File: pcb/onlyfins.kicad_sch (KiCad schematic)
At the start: 47 parts, among them J2 12V_in, Q1 BSS138, U1 L7805

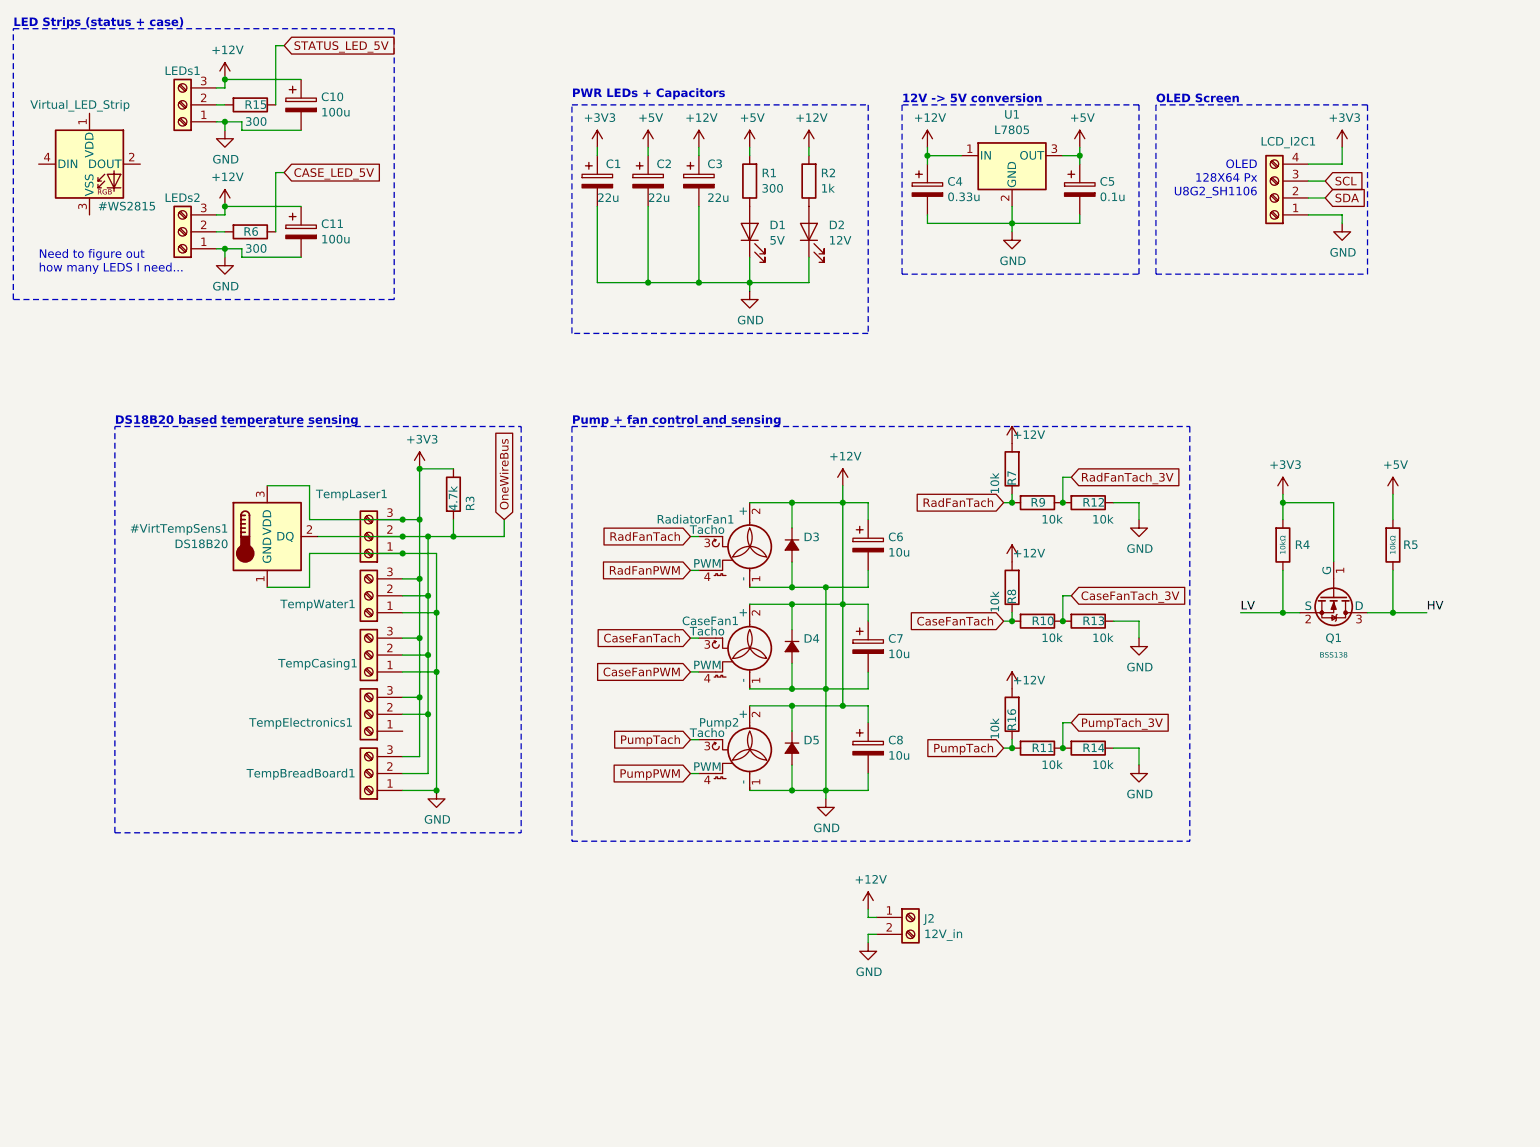
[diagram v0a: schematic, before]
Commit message: Adding subsheets for fan control
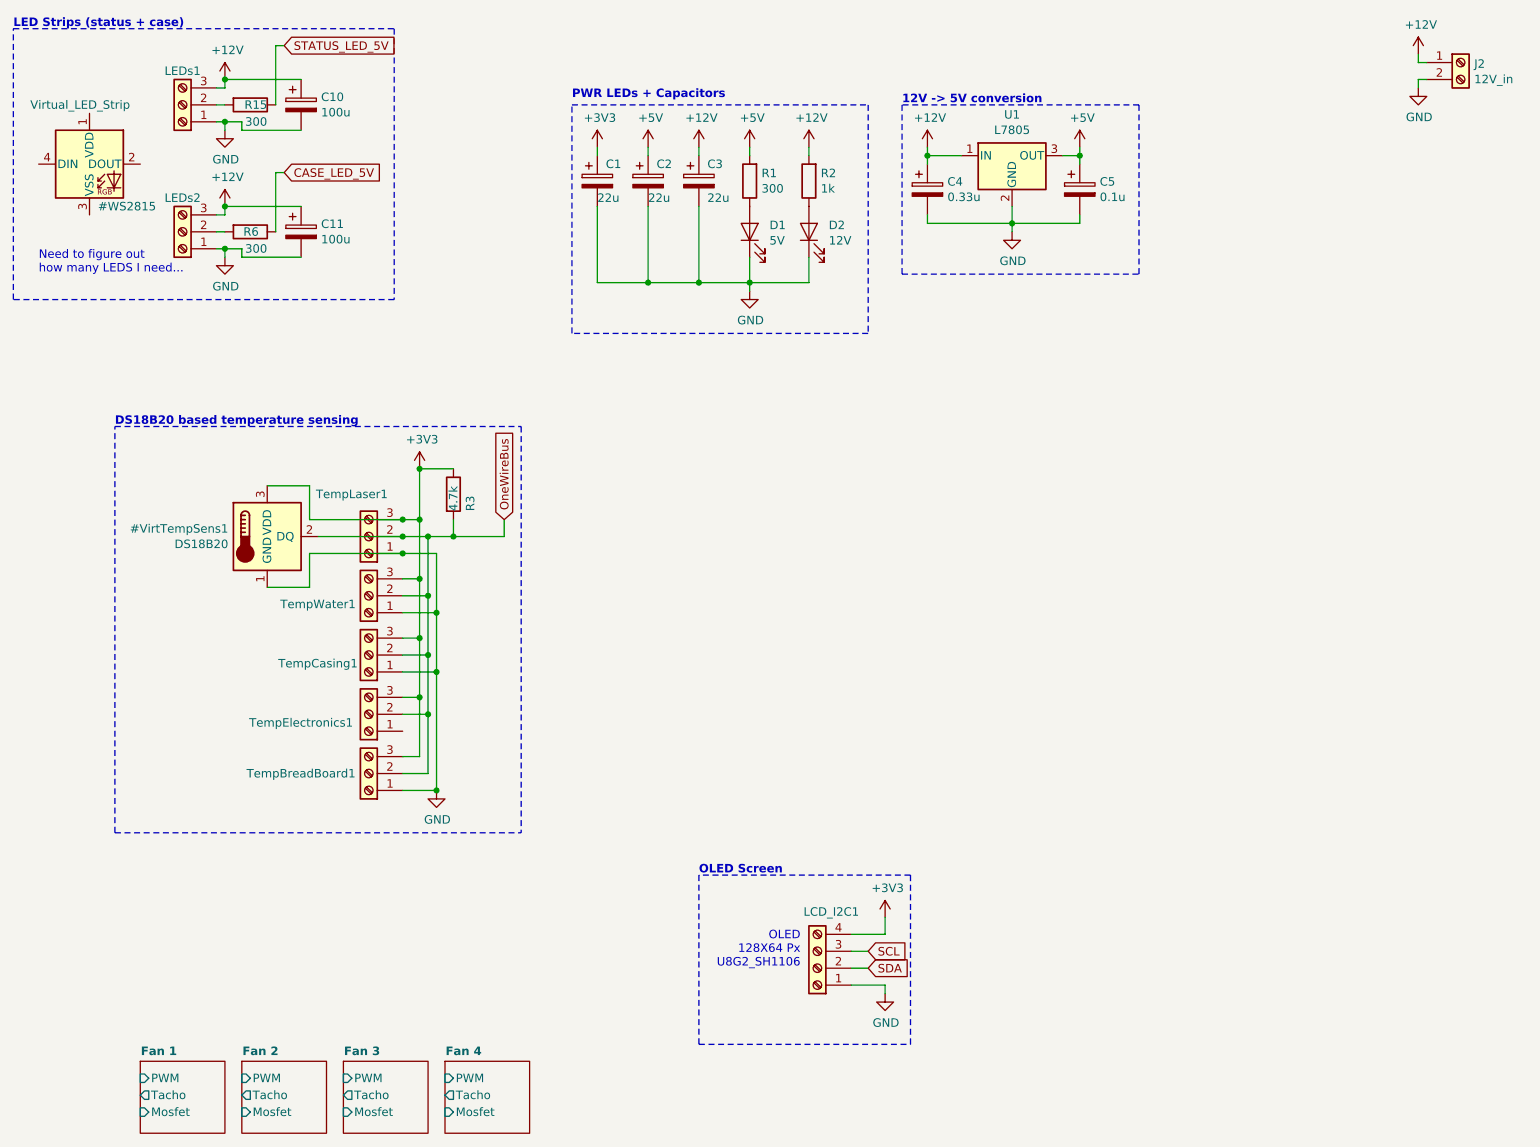
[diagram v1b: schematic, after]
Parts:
- removed C6, C7, C8: 10u, Capacitor_THT:CP_Radial_D5.0mm_P2.50mm, symbol coroam_brains-rescue:CP-Device
- removed CaseFan1, Pump2, RadiatorFan1: Fan_4pin, Connector:FanPinHeader_1x04_P2.54mm_Vertical, symbol coroam_brains-rescue:Fan_4pin-Motor
- removed D3, D4, D5: D_Small_ALT, Diode_SMD:D_SMB_Handsoldering, symbol Device:D_Small_ALT
- removed Q1: BSS138, PCM_JLCPCB:Q_SOT-23, symbol PCM_JLCPCB-Transistors:NMOS,BSS138
- removed R10, R11, R12, R13, R14, R16, R7, R8, R9: 10k, Resistor_SMD:R_2010_5025Metric_Pad1.52x2.65mm_HandSolder, symbol coroam_brains-rescue:R-Device
- removed R4, R5: 10kΩ, PCM_JLCPCB:R_0402, symbol PCM_JLCPCB-Resistors:0402,10kΩ
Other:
- added sheet Fan 1 (fan_control.kicad_sch)
- added sheet Fan 2 (fan_control.kicad_sch)
- added sheet Fan 3 (fan_control.kicad_sch)
- added sheet Fan 4 (fan_control.kicad_sch)
- note removed: "Pump + fan control and sensing"
- moved on the sheet: J2, LCD_I2C1

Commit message: Add temperature sensors
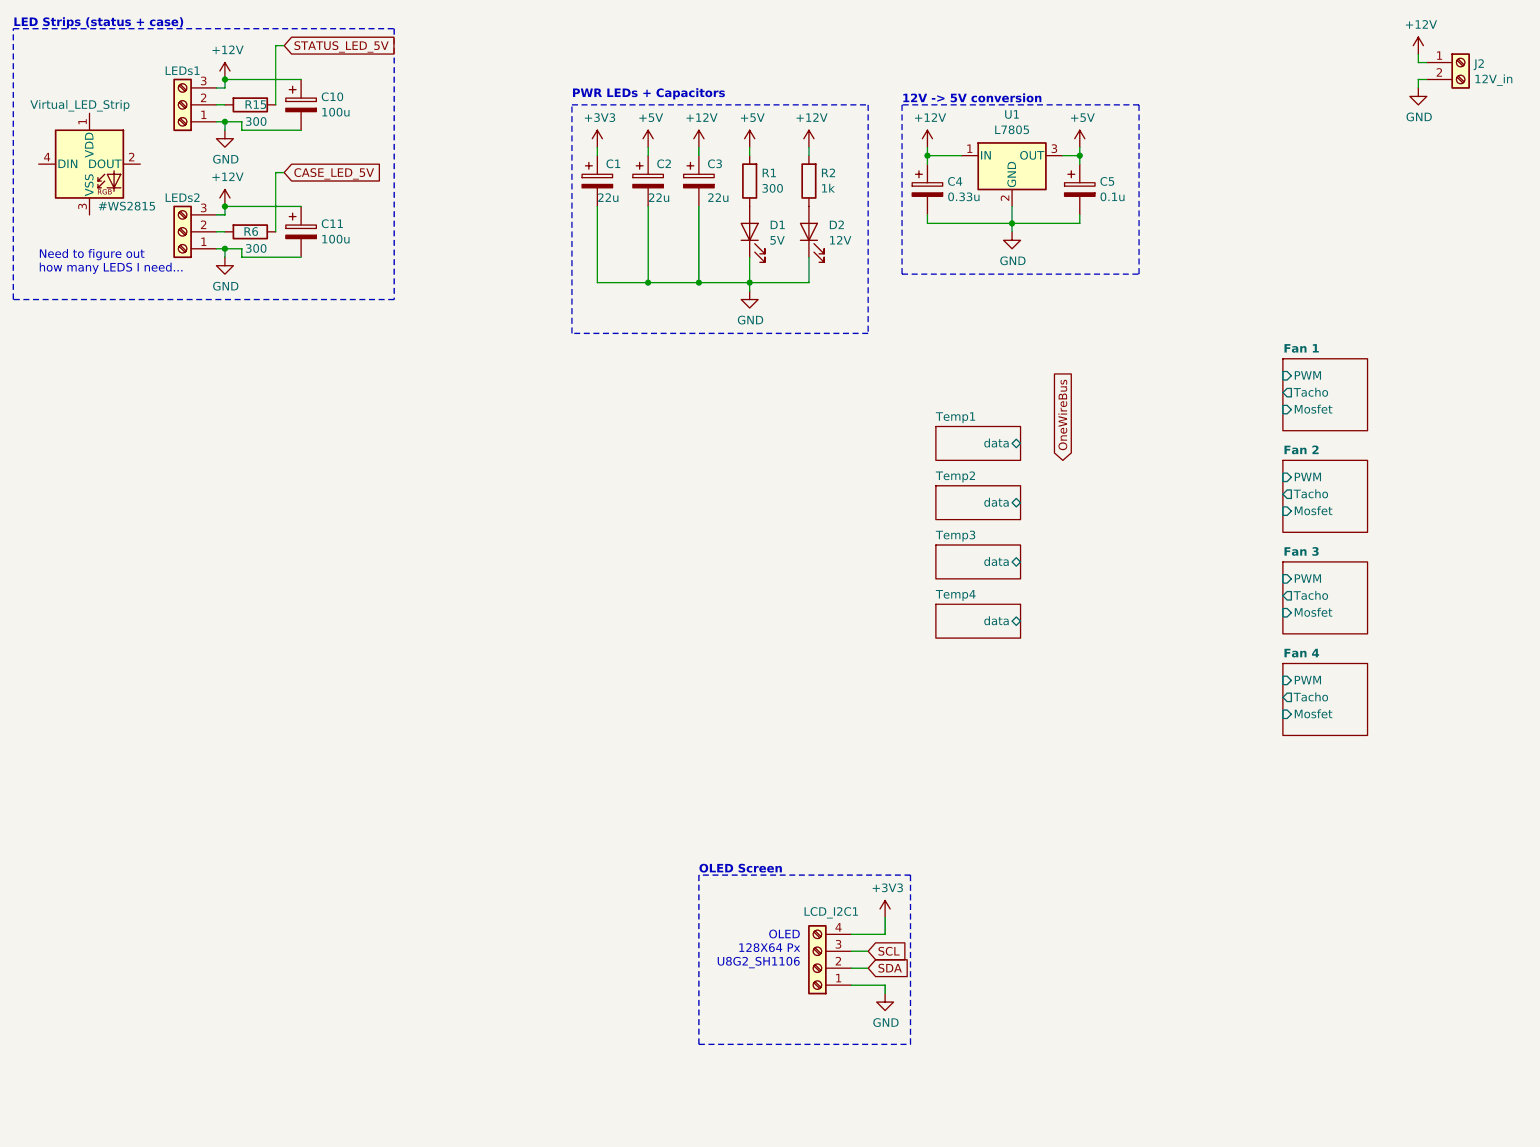
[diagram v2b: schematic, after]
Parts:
- removed #VirtTempSens1: DS18B20, Package_TO_SOT_THT:TO-92_Inline, symbol coroam_brains-rescue:DS18B20-Sensor_Temperature
- removed R3: 4.7k, Resistor_THT:R_Axial_DIN0207_L6.3mm_D2.5mm_P10.16mm_Horizontal, symbol coroam_brains-rescue:R-Device
- removed TempBreadBoard1, TempCasing1, TempElectronics1, TempLaser1, TempWater1: DigiTempSens1, Connector:FanPinHeader_1x03_P2.54mm_Vertical, symbol coroam_brains-rescue:Screw_Terminal_01x03-Connector
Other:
- added sheet Temp1 (one_wire_temp_sensor.kicad_sch)
- added sheet Temp2 (one_wire_temp_sensor.kicad_sch)
- added sheet Temp3 (one_wire_temp_sensor.kicad_sch)
- added sheet Temp4 (one_wire_temp_sensor.kicad_sch)
- note removed: "DS18B20 based temperature sensing"
